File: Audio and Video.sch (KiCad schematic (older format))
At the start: 8 parts, among them M1 Modulator, U170 LM555

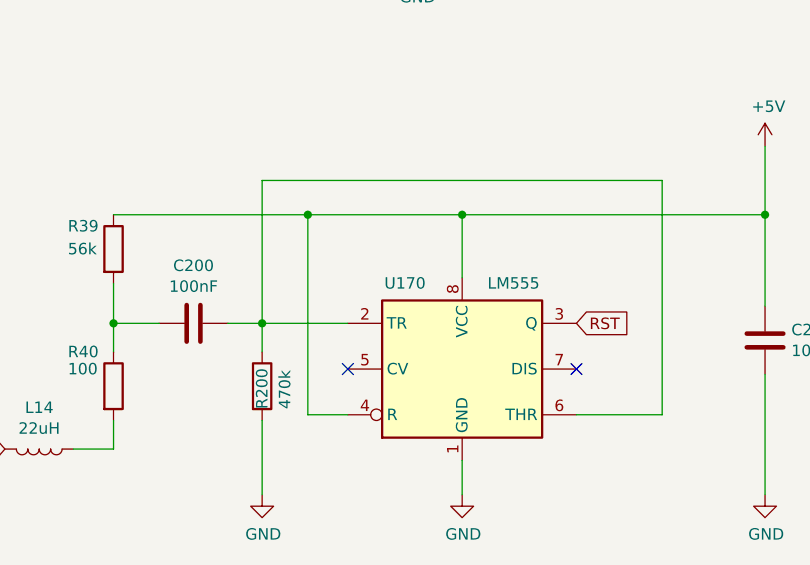
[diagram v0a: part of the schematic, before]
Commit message: Put elements on board
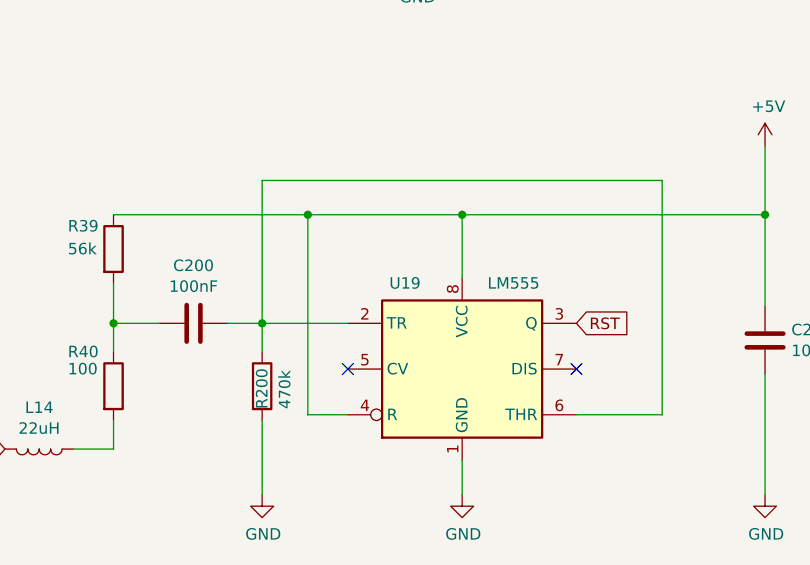
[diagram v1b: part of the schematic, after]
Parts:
- renumbered U170 to U19
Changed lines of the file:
@@
 RF_VCC
 $Comp
-L Timer:LM555 U170
+L Timer:LM555 U19
 U 1 1 602FE634
 P 8425 4450
-F 0 "U170" H 8175 4825 50  0000 C CNN
+F 0 "U19" H 8175 4825 50  0000 C CNN
 F 1 "LM555" H 8650 4825 50  0000 C CNN
 F 2 "Package_DIP:DIP-8_W7.62mm_Socket" H 8425 4450 50  0001 C CNN

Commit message: Schema finished
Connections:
- net +5V renamed +5VA
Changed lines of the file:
@@
 Wire Wire Line
 	7550 4250 7925 4250
-$Comp
-L power:+5V #PWR0201
-U 1 1 603059C3
-P 9750 3475
-F 0 "#PWR0201" H 9750 3325 50  0001 C CNN
-F 1 "+5V" H 9765 3648 50  0000 C CNN
-F 2 "" H 9750 3475 50  0001 C CNN
-F 3 "" H 9750 3475 50  0001 C CNN
-	1    9750 3475
-	1    0    0    -1
-$EndComp
 Wire Wire Line
 	9750 3475 9750 3775
@@
 	6900 4075 6900 4250
 Connection ~ 6900 4250
+$Comp
+L power:+5VA #PWR0201
+U 1 1 6034B357
+P 9750 3475
+F 0 "#PWR0201" H 9750 3325 50  0001 C CNN
+F 1 "+5VA" H 9765 3648 50  0000 C CNN
+F 2 "" H 9750 3475 50  0001 C CNN
+F 3 "" H 9750 3475 50  0001 C CNN
+	1    9750 3475
+	1    0    0    -1
+$EndComp
 $EndSCHEMATC

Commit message: Audio
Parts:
- added C112, C16, C21: 1nF, Atari:C_Axial_L5.1mm_D2.5mm_P12.50mm_Horizontal, symbol Device:C
- added C17, C23: 47nF, Atari:C_Axial_L5.1mm_D2.5mm_P12.50mm_Horizontal, symbol Device:C
- added C19, C20: 4,7uF, Capacitor_THT:CP_Radial_D8.0mm_P3.50mm, symbol Device:C
- added C24: 10uF, Capacitor_THT:C_Axial_L12.0mm_D6.5mm_P15.00mm_Horizontal, symbol Device:CP
- added R1, R11: 2k2, Atari:R_Axial_DIN0207_L3.6mm_D2.2mm_P10.16mm_Horizontal, symbol Device:R
- added R10, R2: 1k, Atari:R_Axial_DIN0207_L3.6mm_D2.2mm_P10.16mm_Horizontal, symbol Device:R
- added R3: 6k2, Atari:R_Axial_DIN0207_L3.6mm_D2.2mm_P10.16mm_Horizontal, symbol Device:R
- added R4: 56k, Atari:R_Axial_DIN0207_L3.6mm_D2.2mm_P10.16mm_Horizontal, symbol Device:R
- added R5: 470k, Atari:R_Axial_DIN0207_L3.6mm_D2.2mm_P10.16mm_Horizontal, symbol Device:R
- added R6: 68k, Atari:R_Axial_DIN0207_L3.6mm_D2.2mm_P10.16mm_Horizontal, symbol Device:R
- added R7: 2k, Atari:R_Axial_DIN0207_L3.6mm_D2.2mm_P10.16mm_Horizontal, symbol Device:R
- added R8: 5k1, Atari:R_Axial_DIN0207_L3.6mm_D2.2mm_P10.16mm_Horizontal, symbol Device:R
- added R9: 3k3, Atari:R_Axial_DIN0207_L3.6mm_D2.2mm_P10.16mm_Horizontal, symbol Device:R
- added U1: LM358, Package_DIP:DIP-8_W7.62mm_Socket, symbol Amplifier_Operational:LM358
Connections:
- net +5VA: now also C16.2, R9.1, U1.8 (V+)
- net GND: now also C112.1, C16.1, C21.1, C24.2, R10.2, R11.2, R3.2, U1.4 (V-)
- net at M1.5 (Audio): now also R6.1, R8.2, U1.1
- new net: R5.2, R6.2, R7.1, U1.2 (-)
- new net: C24.1, R11.1, R9.2, U1.3 (+), U1.5 (+)
- new net: R1.1, R4.1, U1.6 (-)
- new net: R1.2, R2.2, R3.1, U1.7
- new net: C19.1, C20.2, C21.2, R2.1
- new net: C17.1, R4.2
- new net: C20.1, R7.2
- new net: C23.1, R5.1
- new net AUDIO: R10.1, R8.1
- new net BELL: C23.2
- new net SIOAUDIO: C112.2, C19.2
- new net SOUND: C17.2

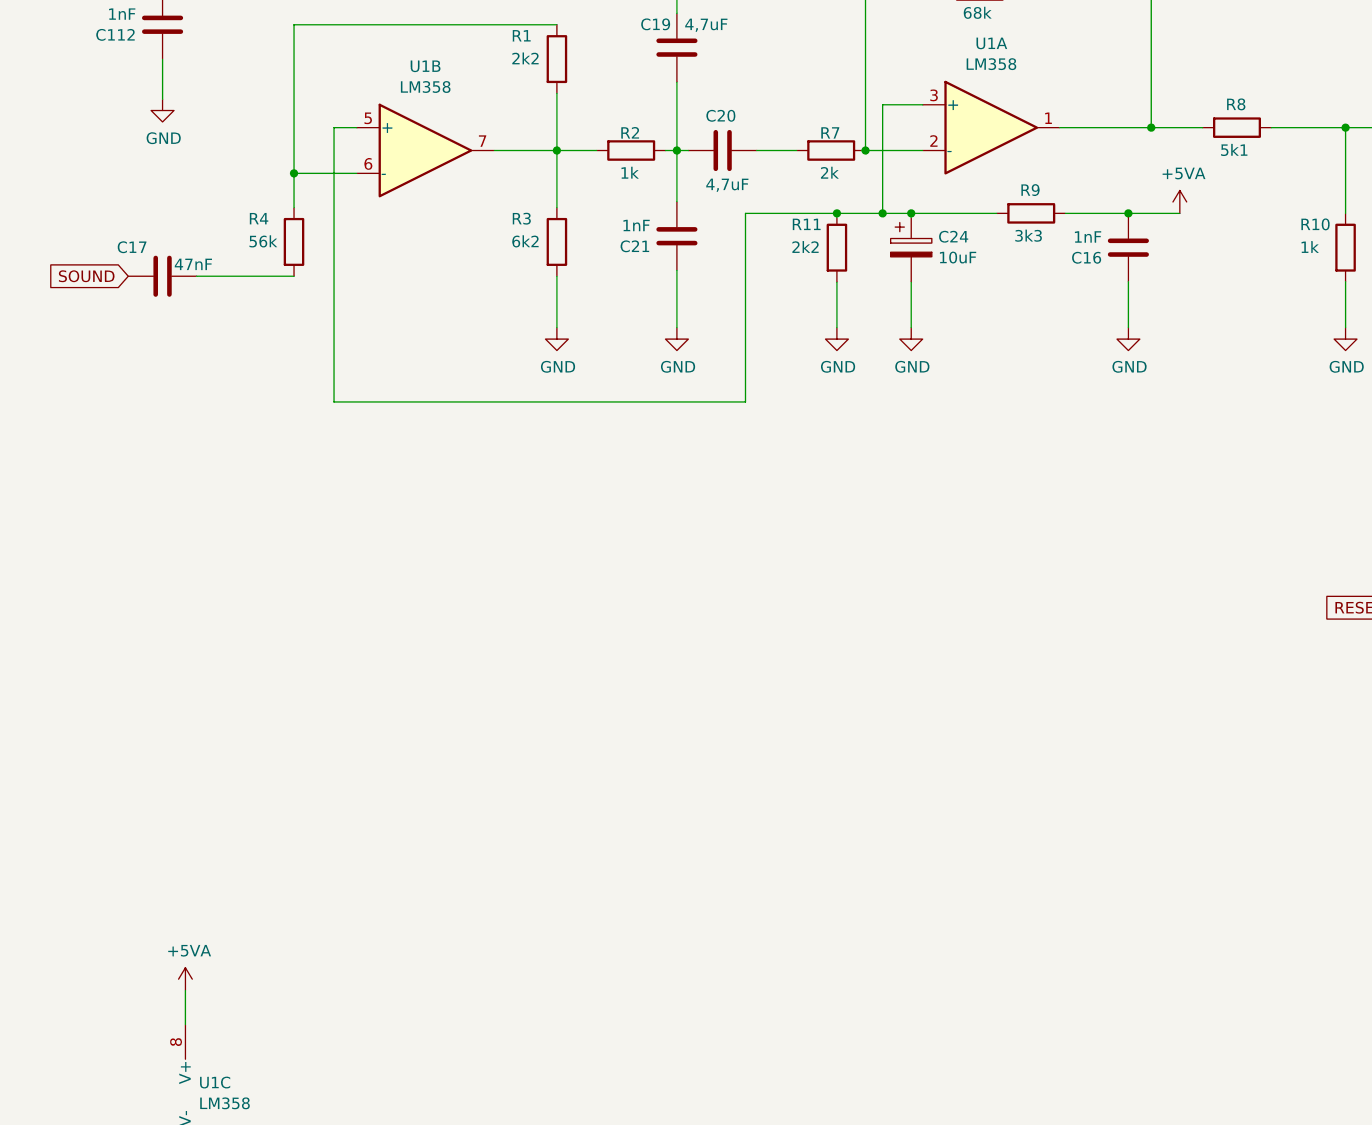
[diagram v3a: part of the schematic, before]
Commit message: Audio put on board
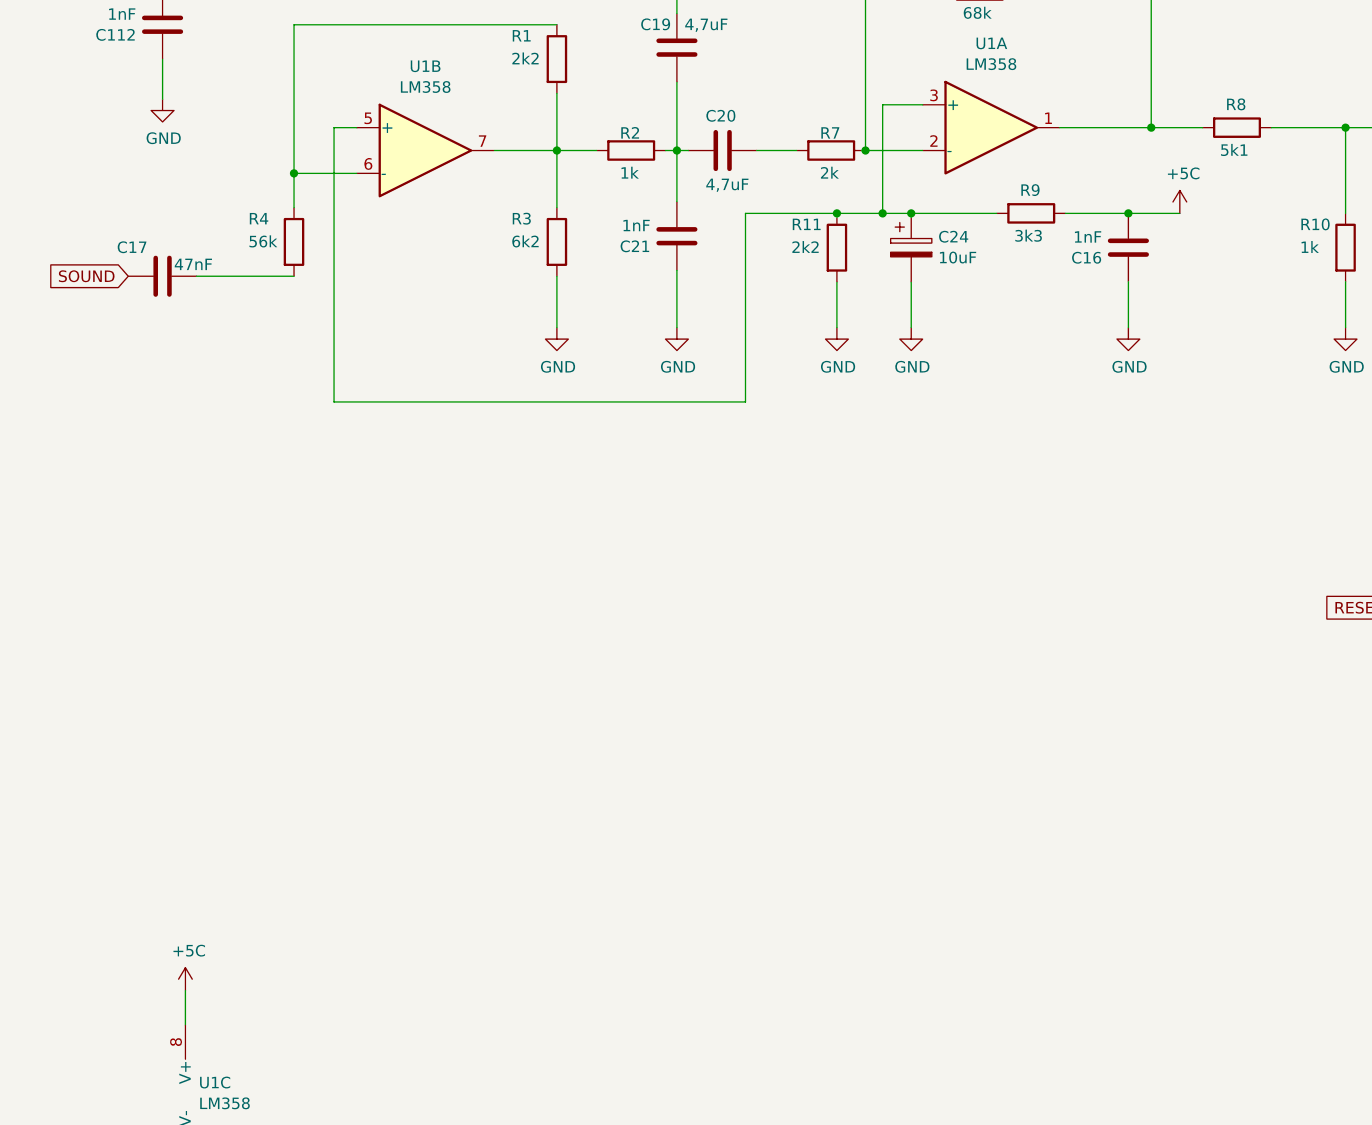
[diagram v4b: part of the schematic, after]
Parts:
- C24: footprint Capacitor_THT:C_Axial_L12.0mm_D6.5mm_P15.00mm_Horizontal -> Capacitor_THT:CP_Axial_L11.0mm_D6.0mm_P18.00mm_Horizontal
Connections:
- net +5VA: no longer C16.2, R9.1, U1.8 (V+)
- new net +5C: C16.2, R9.1, U1.8 (V+)
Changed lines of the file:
@@
 F 0 "C24" H 4418 3271 50  0000 L CNN
 F 1 "10uF" H 4418 3180 50  0000 L CNN
-F 2 "Capacitor_THT:C_Axial_L12.0mm_D6.5mm_P15.00mm_Horizontal" H 4338 3075 50  0001 C CNN
+F 2 "Capacitor_THT:CP_Axial_L11.0mm_D6.0mm_P18.00mm_Horizontal" H 4338 3075 50  0001 C CNN
 F 3 "~" H 4300 3225 50  0001 C CNN
 	1    4300 3225
@@
 Wire Wire Line
 	5250 3375 5250 3575
-$Comp
-L power:+5VA #PWR0245
-U 1 1 60331A6E
+Wire Wire Line
+	1125 6475 1125 6625
+Wire Wire Line
+	5250 3075 5475 3075
+Connection ~ 5250 3075
+$Comp
+L power:+5C #PWR0245
+U 1 1 602CB8CF
+P 5475 3075
+F 0 "#PWR0245" H 5475 2925 50  0001 C CNN
+F 1 "+5C" H 5490 3248 50  0000 C CNN
+F 2 "" H 5475 3075 50  0001 C CNN
+F 3 "" H 5475 3075 50  0001 C CNN
+	1    5475 3075
+	1    0    0    -1
+$EndComp
+$Comp
+L power:+5C #PWR0246
+U 1 1 602CBE97
 P 1125 6475
-F 0 "#PWR0245" H 1125 6325 50  0001 C CNN
-F 1 "+5VA" H 1140 6648 50  0000 C CNN
+F 0 "#PWR0246" H 1125 6325 50  0001 C CNN
+F 1 "+5C" H 1140 6648 50  0000 C CNN
 F 2 "" H 1125 6475 50  0001 C CNN
 F 3 "" H 1125 6475 50  0001 C CNN
@@
 	1    0    0    -1
 $EndComp
-Wire Wire Line
-	1125 6475 1125 6625
-$Comp
-L power:+5VA #PWR0246
-U 1 1 60334249
-P 5475 3075
-F 0 "#PWR0246" H 5475 2925 50  0001 C CNN
-F 1 "+5VA" H 5490 3248 50  0000 C CNN
-F 2 "" H 5475 3075 50  0001 C CNN
-F 3 "" H 5475 3075 50  0001 C CNN
-	1    5475 3075
-	1    0    0    -1
-$EndComp
-Wire Wire Line
-	5250 3075 5475 3075
-Connection ~ 5250 3075
 $EndSCHEMATC

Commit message: Tracking
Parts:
- added FB7: Ferrite_Bead, Atari:L_Axial_L7.0mm_D3.3mm_P12.50mm_Horizontal_Fastron_MICC, symbol Device:Ferrite_Bead
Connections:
- net COMPOSITE: now also FB7.2; no longer M1.1 (Composite)
- net MONO renamed MONO_MOD
- new net: FB7.1, M1.1 (Composite)
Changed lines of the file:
@@
 	0    1    1    0
 $EndComp
-Text GLabel 7825 1500 0    50   Input ~ 0
+Text GLabel 6950 1500 0    50   Input ~ 0
 COMPOSITE
 Text GLabel 7825 1800 0    50   Input ~ 0
 COLOR
 Text GLabel 7825 1950 0    50   Input ~ 0
-MONO
+MONO_MOD
 Wire Wire Line
 	8225 2500 8325 2500
@@
 	1    0    0    -1
 $EndComp
+$Comp
+L Device:Ferrite_Bead FB7
+U 1 1 60348FAD
+P 7100 1500
+F 0 "FB7" V 6826 1500 50  0000 C CNN
+F 1 "Ferrite_Bead" V 6917 1500 50  0000 C CNN
+F 2 "Atari:L_Axial_L7.0mm_D3.3mm_P12.50mm_Horizontal_Fastron_MICC" V 7030 1500 50  0001 C CNN
+F 3 "~" H 7100 1500 50  0001 C CNN
+	1    7100 1500
+	0    1    1    0
+$EndComp
+Wire Wire Line
+	7250 1500 7825 1500
 $EndSCHEMATC

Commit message: Tracking
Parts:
- added C22: 4,7uF, Capacitor_THT:CP_Radial_D8.0mm_P3.50mm, symbol Device:C
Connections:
- net at C19.1, C20.2, C21.2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: now also C22.2
- new net EXTAUDIO: C22.1
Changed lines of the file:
@@
 Wire Wire Line
 	7250 1500 7825 1500
+Text GLabel 875  1625 0    50   Input ~ 0
+EXTAUDIO
+$Comp
+L Device:C C22
+U 1 1 6039DB1C
+P 1275 1625
+F 0 "C22" V 1400 1575 50  0000 L CNN
+F 1 "4,7uF" V 1200 1350 50  0000 L CNN
+F 2 "Capacitor_THT:CP_Radial_D8.0mm_P3.50mm" H 1313 1475 50  0001 C CNN
+F 3 "~" H 1275 1625 50  0001 C CNN
+	1    1275 1625
+	0    -1   -1   0
+$EndComp
+Wire Wire Line
+	875  1625 1125 1625
+Wire Wire Line
+	1425 1625 3675 1625
+Wire Wire Line
+	3675 1625 3675 2500
+Wire Wire Line
+	3675 2500 3275 2500
+Connection ~ 3275 2500
 $EndSCHEMATC

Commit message: Gerber and Tracking
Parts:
- added J106, J107: pin, Connector_PinHeader_2.00mm:PinHeader_1x01_P2.00mm_Vertical, symbol Connector_Generic:Conn_01x01
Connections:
- net BELL: now also J106.1 (Pin_1)
- net at C17.1, R4.2: now also J107.1 (Pin_1)
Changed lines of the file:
@@
 $EndComp
 Wire Wire Line
-	1175 3350 1600 3350
+	1175 3350 1200 3350
 Text GLabel 875  3350 0    50   Input ~ 0
 SOUND
@@
 BELL
 Wire Wire Line
-	3475 1400 850  1400
+	3475 1400 3325 1400
 $Comp
 L power:GND #PWR0243
@@
 	3675 2500 3275 2500
 Connection ~ 3275 2500
+$Comp
+L Connector_Generic:Conn_01x01 J106
+U 1 1 604383A6
+P 3325 900
+F 0 "J106" V 3289 812 50  0000 R CNN
+F 1 "pin" V 3198 812 50  0000 R CNN
+F 2 "Connector_PinHeader_2.00mm:PinHeader_1x01_P2.00mm_Vertical" H 3325 900 50  0001 C CNN
+F 3 "~" H 3325 900 50  0001 C CNN
+	1    3325 900
+	0    -1   -1   0
+$EndComp
+Wire Wire Line
+	3325 1100 3325 1400
+Connection ~ 3325 1400
+Wire Wire Line
+	3325 1400 850  1400
+$Comp
+L Connector_Generic:Conn_01x01 J107
+U 1 1 6044E0CA
+P 1200 3800
+F 0 "J107" V 1072 3880 50  0000 L CNN
+F 1 "pin" V 1163 3880 50  0000 L CNN
+F 2 "Connector_PinHeader_2.00mm:PinHeader_1x01_P2.00mm_Vertical" H 1200 3800 50  0001 C CNN
+F 3 "~" H 1200 3800 50  0001 C CNN
+	1    1200 3800
+	0    1    1    0
+$EndComp
+Wire Wire Line
+	1200 3600 1200 3350
+Connection ~ 1200 3350
+Wire Wire Line
+	1200 3350 1600 3350
 $EndSCHEMATC
